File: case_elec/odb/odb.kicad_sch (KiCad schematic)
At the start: 10 parts, among them J1 Screw_Terminal_01x02, J2 Conn_02x07_Top_Bottom, SW1 SW_SPST, SW2 SW_SPST, U1 REYAX RYLR896, U2 BNO055, U3 MPL3115A, U4 Ultimate_GPS, U5 Teensy3.5

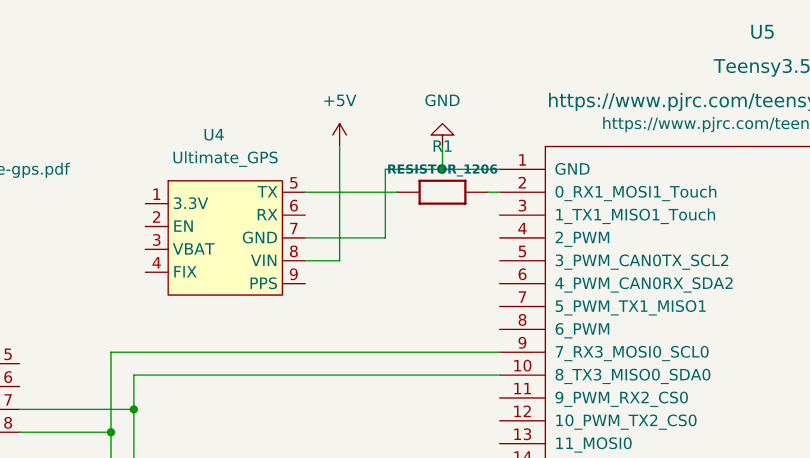
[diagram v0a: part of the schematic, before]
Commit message: Ajout de pistes B.Cu
Alternative à :
- resistances 0 Ohm
- modification du pinout de la Teensy 3.5

Attention : les gerbers n'ont pas été générés.
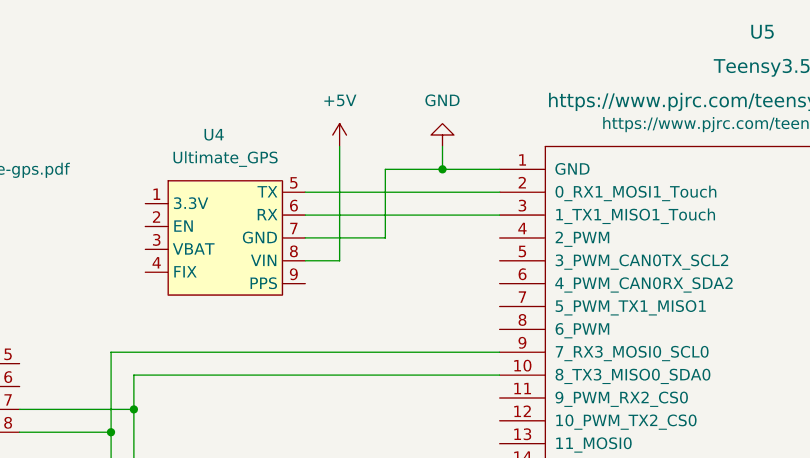
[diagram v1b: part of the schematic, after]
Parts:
- removed R1: RESISTOR_1206, Resistor_SMD:R_1206_3216Metric_Pad1.30x1.75mm_HandSolder, symbol odb-eagle-import:RESISTOR_1206
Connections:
- net at U5.2 (0_RX1_MOSI1_Touch): now also U4.5 (TX)
- net at U5.3 (1_TX1_MISO1_Touch): now also U4.6 (RX)
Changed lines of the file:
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@@
     (stroke (width 0) (type default) (color 0 0 0 0))
   )
-  (wire (pts (xy 149.86 36.83) (xy 151.13 36.83))
-    (stroke (width 0) (type default) (color 0 0 0 0))
-  )
-  (wire (pts (xy 129.54 36.83) (xy 139.7 36.83))
+  (wire (pts (xy 129.54 36.83) (xy 151.13 36.83))
     (stroke (width 0) (type default) (color 0 0 0 0))
   )
@@
   )
   (wire (pts (xy 209.55 138.43) (xy 213.36 138.43))
+    (stroke (width 0) (type default) (color 0 0 0 0))
+  )
+  (wire (pts (xy 129.54 39.37) (xy 151.13 39.37))
     (stroke (width 0) (type default) (color 0 0 0 0))
   )
@@
     (pin "2")
   )
-  (symbol (lib_id "odb-eagle-import:RESISTOR_1206") (at 144.78 36.83 0) (unit 1)
-    (in_bom yes) (on_board yes) (fields_autoplaced)
-    (property "Reference" "R1" (id 0) (at 144.78 31.75 0))
-    (property "Value" "RESISTOR_1206" (id 1) (at 144.78 34.29 0)
-      (effects (font (size 1.016 1.016) bold))
-    )
-    (property "Footprint" "Resistor_SMD:R_1206_3216Metric_Pad1.30x1.75mm_HandSolder" (id 2) (at 144.78 36.83 0)
-      (effects (font (size 1.27 1.27)) hide)
-    )
-    (property "Datasheet" "" (id 3) (at 144.78 36.83 0)
-      (effects (font (size 1.27 1.27)) hide)
-    )
-    (pin "1")
-    (pin "2")
-  )
   (symbol (lib_id "reyax_rylr896:REYAX RYLR896") (at 59.69 135.89 0) (mirror y) (unit 1)
     (in_bom yes) (on_board yes)
@@
       (reference "J2") (unit 1) (value "Conn_02x07_Top_Bottom") (footprint "Connector_Molex:Molex_Nano-Fit_105310-xx14_2x07_P2.50mm_Vertical")
     )
-    (path "/92122d1f-5730-4015-aa36-a6febc7e4df1"
-      (reference "R1") (unit 1) (value "RESISTOR_1206") (footprint "Resistor_SMD:R_1206_3216Metric_Pad1.30x1.75mm_HandSolder")
-    )
     (path "/9077b56f-c102-47b4-9a60-c432e96c7e85"
